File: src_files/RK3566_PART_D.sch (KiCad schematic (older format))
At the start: 29 parts, among them U1 RK3566, U4 LPDDRS_32_IS43LQ32128A-062BLI, Y3 24MHz/10ppm

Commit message: all screens added_3 items left
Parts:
- gave numbers to parts that had none: 6
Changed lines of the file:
@@
 $Descr A3 16535 11693
 encoding utf-8
-Sheet 10 11
+Sheet 10 12
 Title ""
 Date ""
@@
 	8925 9950 8925 9850
 $Comp
-L Device:R_US R?
+L Device:R_US R49
 U 1 1 6243D32E
 P 9325 10125
-F 0 "R?" V 9250 10100 50  0000 C CNN
+F 0 "R49" V 9250 10100 50  0000 C CNN
 F 1 "2.2K_5%" V 9400 10125 50  0000 C CNN
 F 2 "Resistor_SMD:R_0402_1005Metric" V 9365 10115 50  0001 C CNN
@@
 $EndComp
 $Comp
-L Device:R_US R?
+L Device:R_US R48
 U 1 1 62422541
 P 8925 10100
-F 0 "R?" V 8850 10075 50  0000 C CNN
+F 0 "R48" V 8850 10075 50  0000 C CNN
 F 1 "2.2K_5%" V 9000 10100 50  0000 C CNN
 F 2 "Resistor_SMD:R_0402_1005Metric" V 8965 10090 50  0001 C CNN
@@
 	9950 9925 9950 9825
 $Comp
-L Device:R_US R?
+L Device:R_US R51
 U 1 1 626F2B0D
 P 10350 10100
-F 0 "R?" V 10275 10075 50  0000 C CNN
+F 0 "R51" V 10275 10075 50  0000 C CNN
 F 1 "2.2K_5%" V 10425 10100 50  0000 C CNN
 F 2 "Resistor_SMD:R_0402_1005Metric" V 10390 10090 50  0001 C CNN
@@
 $EndComp
 $Comp
-L Device:R_US R?
+L Device:R_US R50
 U 1 1 626F2B17
 P 9950 10075
-F 0 "R?" V 9875 10050 50  0000 C CNN
+F 0 "R50" V 9875 10050 50  0000 C CNN
 F 1 "2.2K_5%" V 10025 10075 50  0000 C CNN
 F 2 "Resistor_SMD:R_0402_1005Metric" V 9990 10065 50  0001 C CNN
@@
 	10725 9900 10725 9800
 $Comp
-L Device:R_US R?
+L Device:R_US R53
 U 1 1 6277A9D8
 P 11125 10075
-F 0 "R?" V 11050 10050 50  0000 C CNN
+F 0 "R53" V 11050 10050 50  0000 C CNN
 F 1 "2.2K_5%" V 11200 10075 50  0000 C CNN
 F 2 "Resistor_SMD:R_0402_1005Metric" V 11165 10065 50  0001 C CNN
@@
 $EndComp
 $Comp
-L Device:R_US R?
+L Device:R_US R52
 U 1 1 6277A9E2
 P 10725 10050
-F 0 "R?" V 10650 10025 50  0000 C CNN
+F 0 "R52" V 10650 10025 50  0000 C CNN
 F 1 "2.2K_5%" V 10800 10050 50  0000 C CNN
 F 2 "Resistor_SMD:R_0402_1005Metric" V 10765 10040 50  0001 C CNN

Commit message: update NFC, 5G, GPS__left LiPo charger+screen changes
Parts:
- added D?: 1N5819WS, Diode_SMD:D_SOD-323, symbol Device:D
- added D? (x2): ESD5451R-2/TR, greencharge-footprints:DFP1006-2L, symbol Device:D_TVS
- added D?: SMF11A, Diode_SMD:D_SOD-123, symbol dk_TVS-Diodes:ESD5Z3_3T1G
- added R?: 22R, symbol Device:R_US
- added R?: 100R, symbol Device:R_US
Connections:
- net GND: now also D?.2 (A2), D?.2 (A2), D?.A
- net VCC3V3_PMU: now also U1.1V19 (GPIO0_D0_u), D?.2 (A)
- net UART2_TX_M0_DEBUG: now reaches U1.1U18 (GPIO0_D1_u)
- net UART2_TX_M0_DEBUG: now also D?.K, R?.1
- new net: D?.1 (K), R?.1
- new net: D?.1 (A1), R?.2 (x2)
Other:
- note added: "UART_DEBUG"
- moved on the sheet: C84, C85, C86, C87, C88, C89, C90, C91, C92, C93, C94, C95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

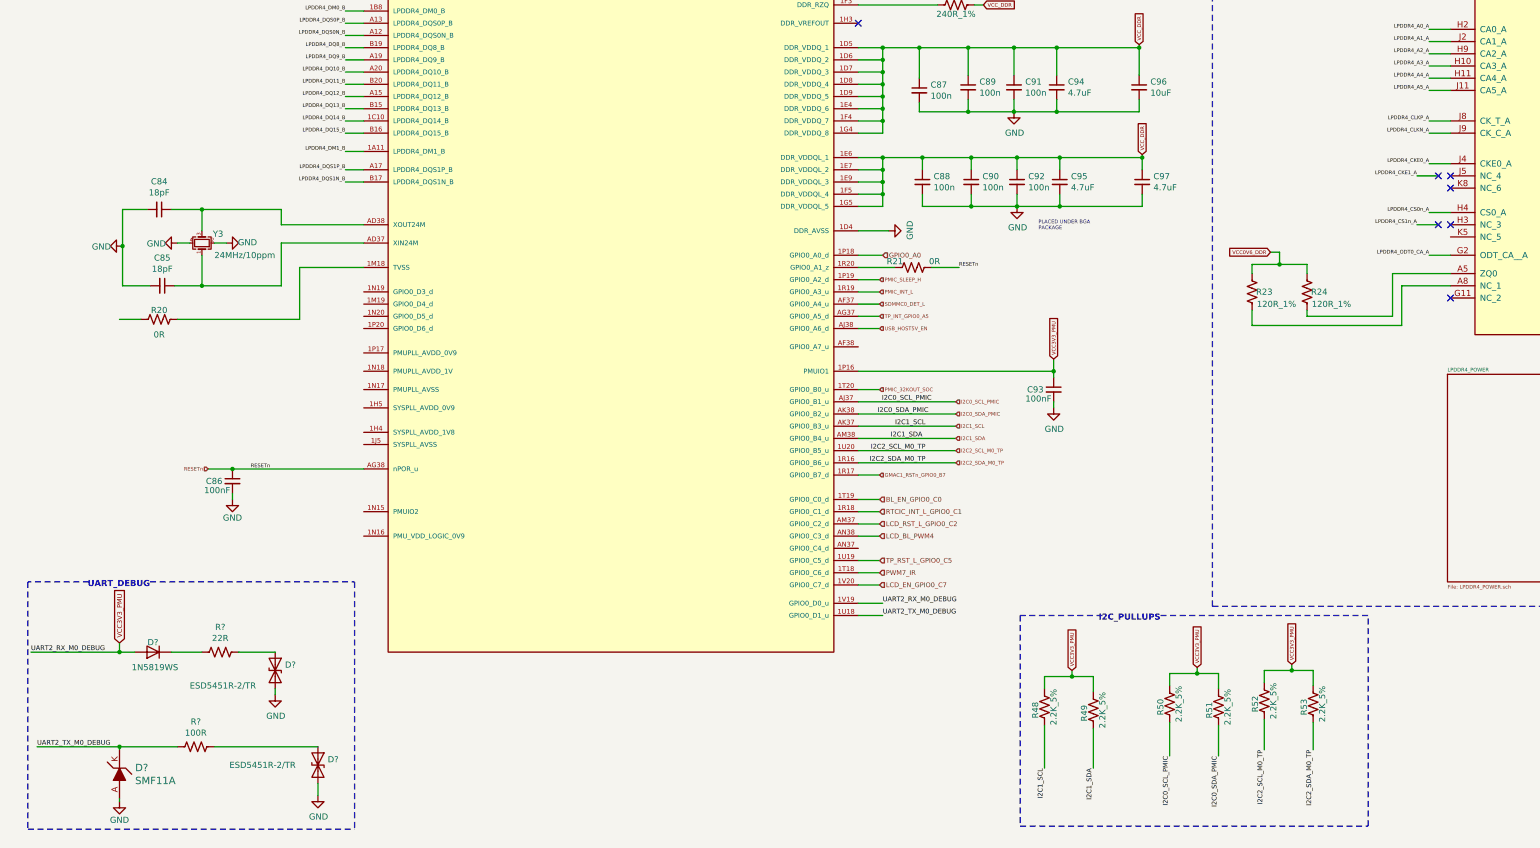
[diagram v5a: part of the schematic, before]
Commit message: schematic capture complete
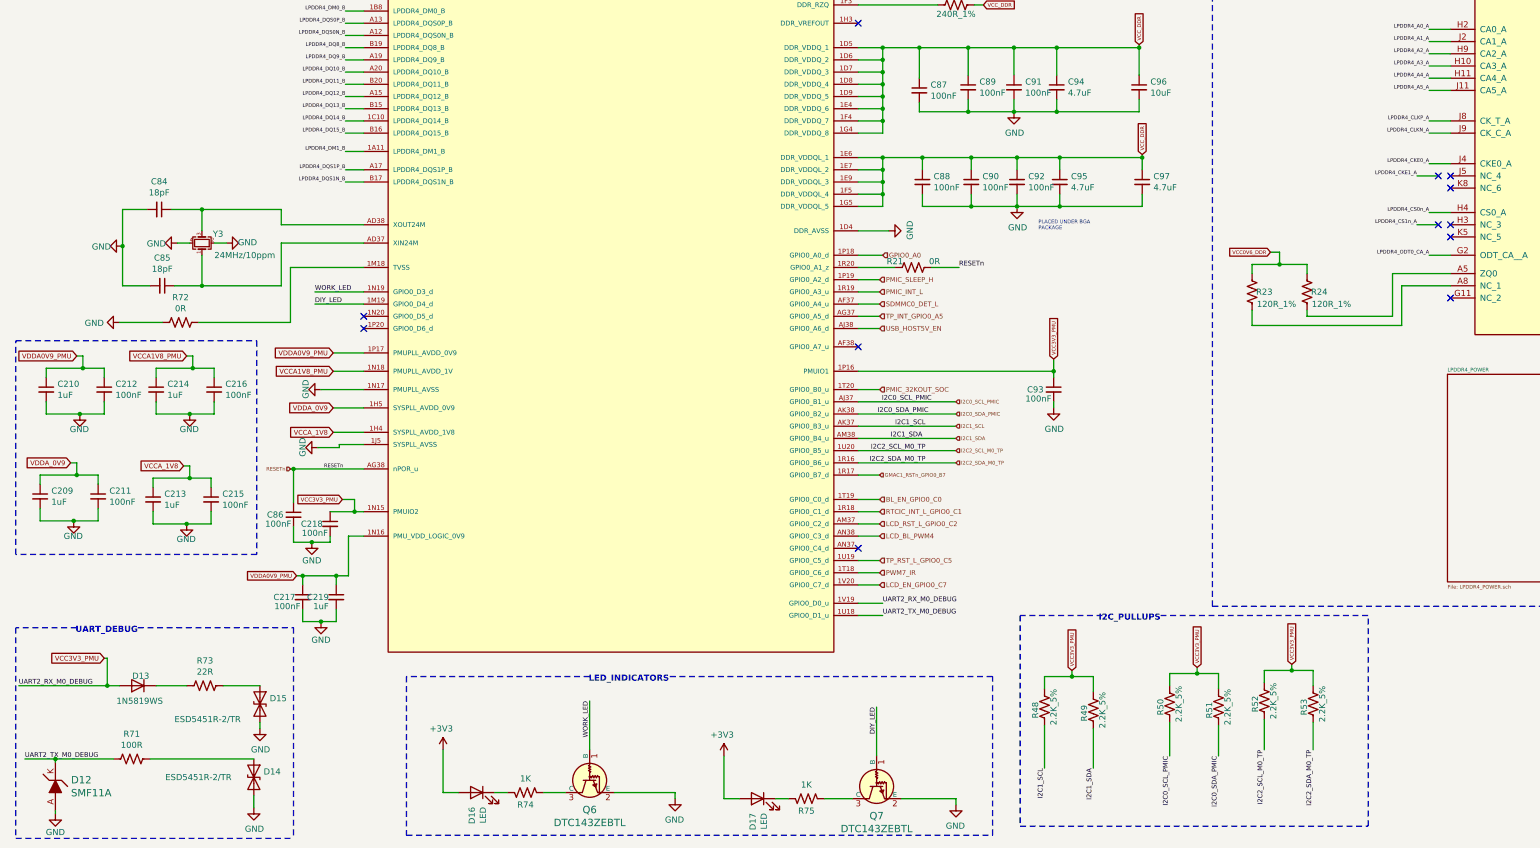
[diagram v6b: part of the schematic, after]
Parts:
- removed R20: 0R, Resistor_SMD:R_0402_1005Metric, symbol Device:R_US
- added C209, C210, C213, C214, C219: 1uF, Capacitor_SMD:C_0402_1005Metric, symbol Device:C_Small
- added C211, C212, C215, C216, C217, C218: 100nF, Capacitor_SMD:C_0402_1005Metric, symbol Device:C_Small
- added D16, D17: LED, LED_SMD:LED_0603_1608Metric, symbol Device:LED
- added Q6, Q7: DTC143ZEBTL, greencharge-footprints:SOTFL50P160X85-3N, symbol dk_Transistors-Bipolar-BJT-Single-Pre-Biased:MMUN2211LT1G
- added R72: 0R, Resistor_SMD:R_0402_1005Metric, symbol Device:R_US
- added R74, R75: 1K, Resistor_SMD:R_0402_1005Metric, symbol Device:R_US
- C87, C88, C89, C90, C91, C92: value 100n -> 100nF
- R71: renamed from R?; footprint (none) -> Resistor_SMD:R_0402_1005Metric_Pad0.72x0.64mm_HandSolder
- R73: renamed from R?; footprint (none) -> Resistor_SMD:R_0402_1005Metric
- Y3: footprint Crystal:Crystal_SMD_3225-4Pin_3.2x2.5mm_HandSoldering -> Crystal:Crystal_SMD_2016-4Pin_2.0x1.6mm; MPN (none) -> ABM11W-24.0000MHZ-7-K1Z-T3
- gave numbers to parts that had none: 4
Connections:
- net GND: now also U1.1J5 (SYSPLL_AVSS), U1.1N17 (PMUPLL_AVSS), C209.2, C210.2, C211.2, C212.2, C213.2, C214.2, C215.2, C216.2, C217.2, C218.2, C219.2, Q6.2 (E), Q7.2 (E), R72.2
- net VCC3V3_PMU: now also U1.1N15 (PMUIO2), C218.1
- net at U1.1M18 (TVSS): now also R72.1
- net VCCA_1V8: now reaches U1.1H4 (SYSPLL_AVDD_1V8)
- net VCCA_1V8: now also C213.1, C215.1
- net VDDA_0V9: now reaches U1.1H5 (SYSPLL_AVDD_0V9)
- net VDDA_0V9: now also C209.1, C211.1
- net DIY_LED: now reaches U1.1M19 (GPIO0_D4_d)
- net DIY_LED: now also Q7.1 (B)
- net VDDA0V9_PMU: now reaches U1.1N16 (PMU_VDD_LOGIC_0V9)
- net VDDA0V9_PMU: now also U1.1P17 (PMUPLL_AVDD_0V9), C210.1, C212.1, C217.1, C219.1
- net VCCA1V8_PMU: now reaches U1.1N18 (PMUPLL_AVDD_1V)
- net VCCA1V8_PMU: now also C214.1, C216.1
- net WORK_LED: now reaches U1.1N19 (GPIO0_D3_d)
- net WORK_LED: now also Q6.1 (B)
- new net: D17.1 (K), R75.1
- new net: Q7.3 (C), R75.2
- new net: D16.1 (K), R74.1
- new net: Q6.3 (C), R74.2
- new net +3V3: D16.2 (A), D17.2 (A)
- no-connect marks 16 -> 21
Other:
- note added: "LED_INDICATORS"
- moved on the sheet: C86, D12, D13, D14, D15, R71, R73

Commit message: updated footprint and schematics
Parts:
- U1: footprint greencharge-footprints:BGA828C65P31X31_2100X2100X161N -> greencharge-footprints:RK366_BGA-565_20x18_15.5x14.4mm
- U4: value LPDDRS_32_IS43LQ32128A-062BLI -> LPDDR4_32_IS43LQ32128A-062BLI
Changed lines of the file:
@@
 $Descr A3 16535 11693
 encoding utf-8
-Sheet 8 15
+Sheet 8 16
 Title ""
 Date ""
@@
 P 13950 1250
 F 0 "U4" H 13475 1128 30  0000 C CNN
-F 1 "LPDDRS_32_IS43LQ32128A-062BLI" H 13475 1068 30  0000 C CNN
+F 1 "LPDDR4_32_IS43LQ32128A-062BLI" H 13475 1068 30  0000 C CNN
 F 2 "greencharge-footprints:BGA200C65P12X22_1000X1450X85" H 13500 950 30  0001 C CNN
 F 3 "" H 13500 950 30  0001 C CNN
@@
 F 0 "U1" H 5350 -125 50  0000 C CNN
 F 1 "RK3566" H 5375 -200 50  0000 C CNN
-F 2 "greencharge-footprints:BGA828C65P31X31_2100X2100X161N" H 4800 150 50  0001 C CNN
+F 2 "greencharge-footprints:RK366_BGA-565_20x18_15.5x14.4mm" H 4800 150 50  0001 C CNN
 F 3 "" H 4800 150 50  0001 C CNN
 	2    5350 250
